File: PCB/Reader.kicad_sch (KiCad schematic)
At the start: 43 parts, among them J1 Conn_01x04, J2 Amphenol Dubox ‎76383-402LF‎, J3 Conn_01x04, J4 Conn_01x08, J5 Conn_01x10, J6 Conn_01x03, J7 Conn_01x02, Q1 2N7002, Q2 2N7002, Q3 2N7002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

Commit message: Replace LED resistor values with lookup table
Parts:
- R1, R2, R8: value 100R -> ~
- R7: value 200R -> ~
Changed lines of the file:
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@@
 			)
 		)
-		(property "Value" "100R"
+		(property "Value" "~"
 			(at 154.178 26.543 0)
 			(effects
@@
 			)
 		)
-		(property "Value" "200R"
+		(property "Value" "~"
 			(at 154.178 79.883 0)
 			(effects
@@
 			)
 		)
-		(property "Value" "100R"
+		(property "Value" "~"
 			(at 213.868 26.543 0)
 			(effects
@@
 			)
 		)
-		(property "Value" "100R"
+		(property "Value" "~"
 			(at 202.438 79.883 0)
 			(effects

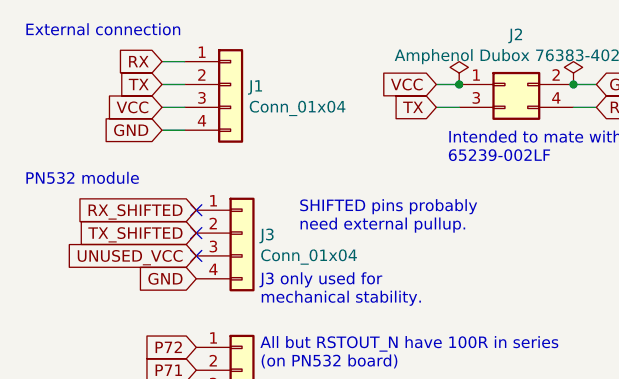
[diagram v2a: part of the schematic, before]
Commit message: Mark 4-pin J1 pin header as DNP
This pin header is an alternative for the J2 2x2 pin connector and the
footprint is added just in case, but normally only J2 should be used.
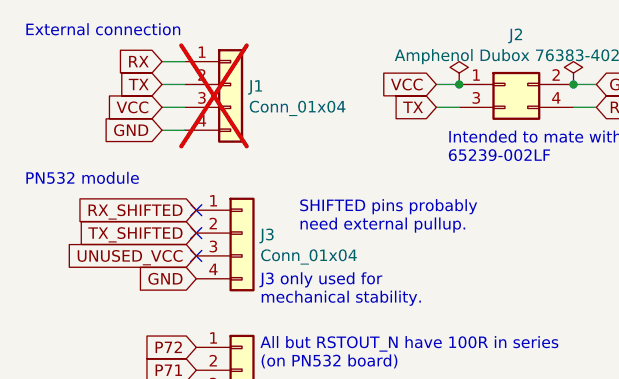
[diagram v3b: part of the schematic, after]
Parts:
- J1: now not fitted
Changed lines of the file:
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@@
 		(in_bom yes)
 		(on_board yes)
-		(dnp no)
+		(dnp yes)
 		(property "Reference" "J1"
 			(at 40.132 20.5232 0)

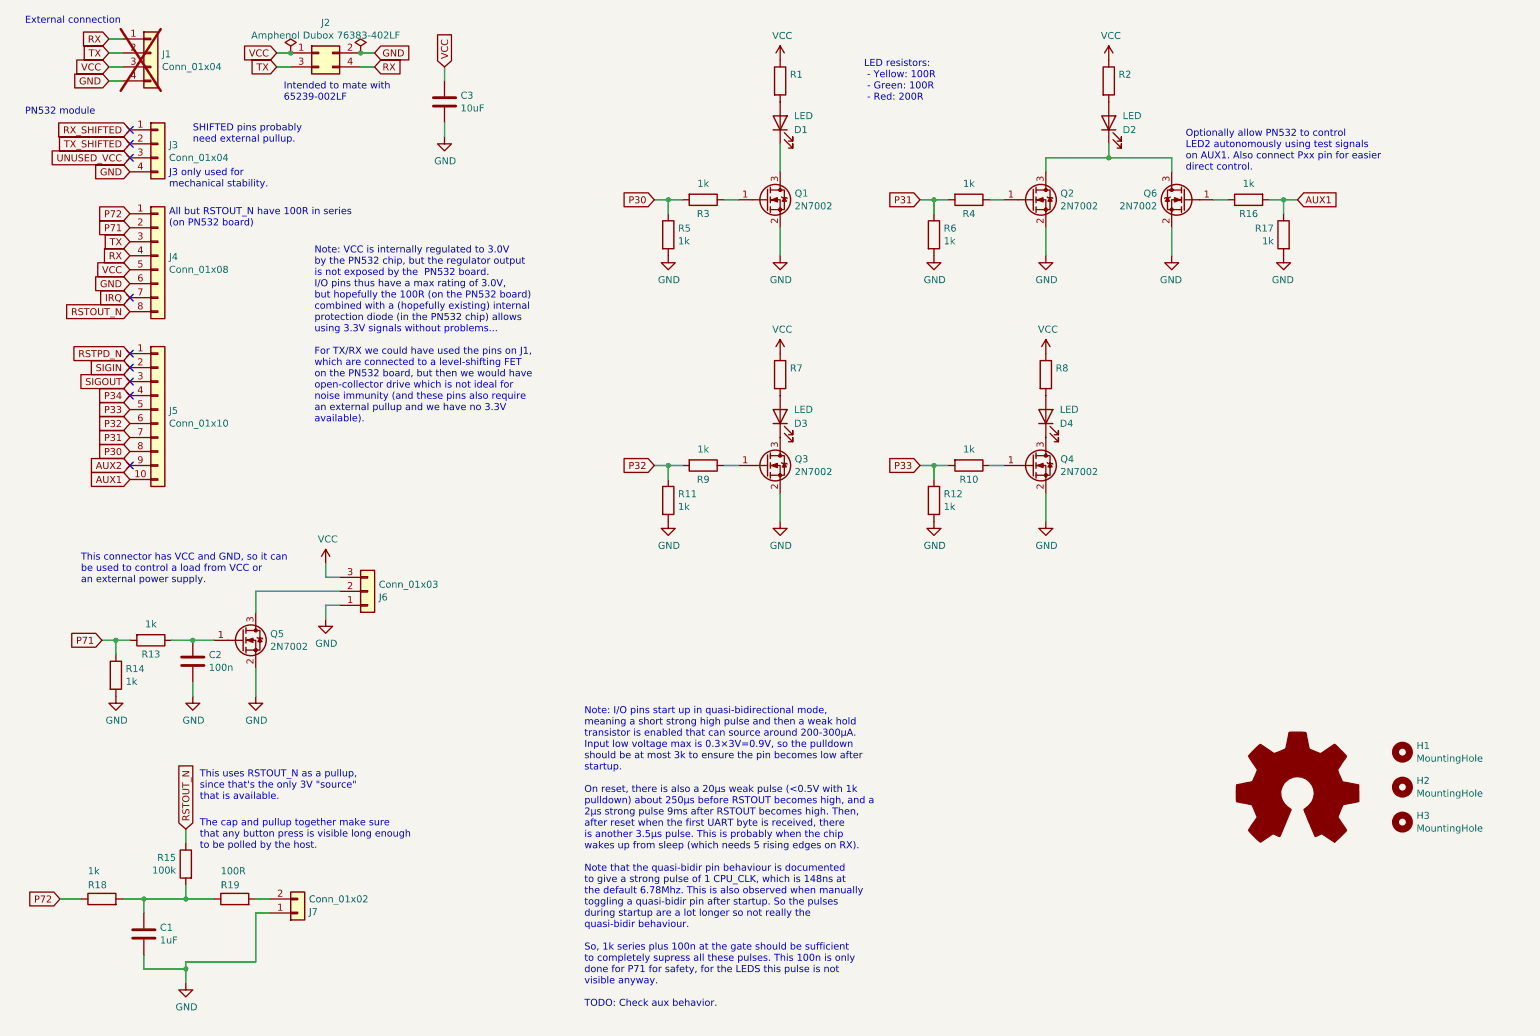
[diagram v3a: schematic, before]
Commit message: Add some (estethic) structure to the schematic
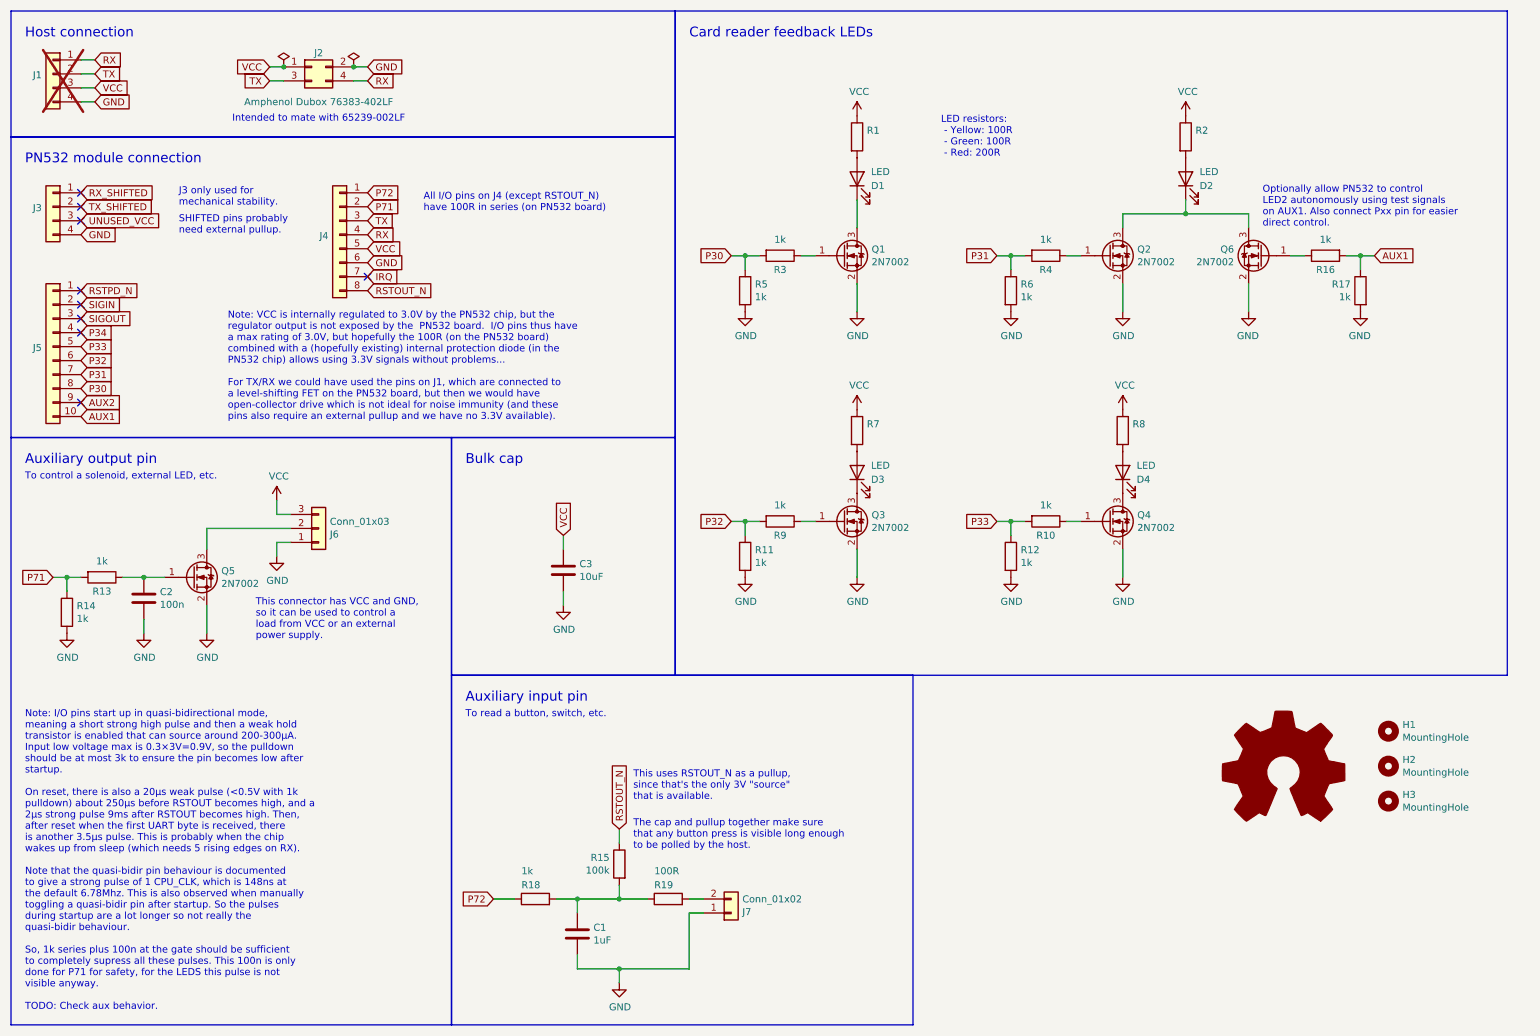
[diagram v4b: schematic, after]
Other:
- note added: "All I/O pins on J4 (except RSTOUT_N) have 100R in series (on PN532 board)"
- note added: "Auxiliary input pin"
- note added: "Auxiliary output pin"
- note added: "Bulk cap"
- note added: "Card reader feedback LEDs"
- note added: "Host connection"
- note added: "PN532 module connection"
- note added: "To control a solenoid, external LED, etc."
- note added: "To read a button, switch, etc."
- note removed: "All but RSTOUT_N have 100R in series (on PN532 board)"
- note removed: "External connection"
- note removed: "PN532 module"
- moved on the sheet: C1, C2, C3, D1, D2, D3, D4, H1, H2, H3, J1, J2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
